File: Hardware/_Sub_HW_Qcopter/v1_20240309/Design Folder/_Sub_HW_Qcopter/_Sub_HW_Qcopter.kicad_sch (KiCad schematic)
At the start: 0 parts

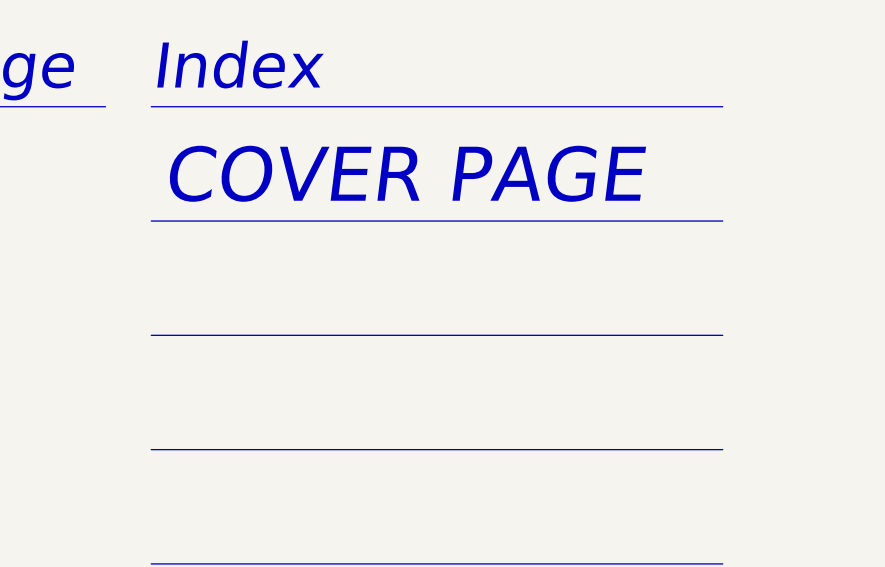
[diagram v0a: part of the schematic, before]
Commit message: The document structure of hardware has been added
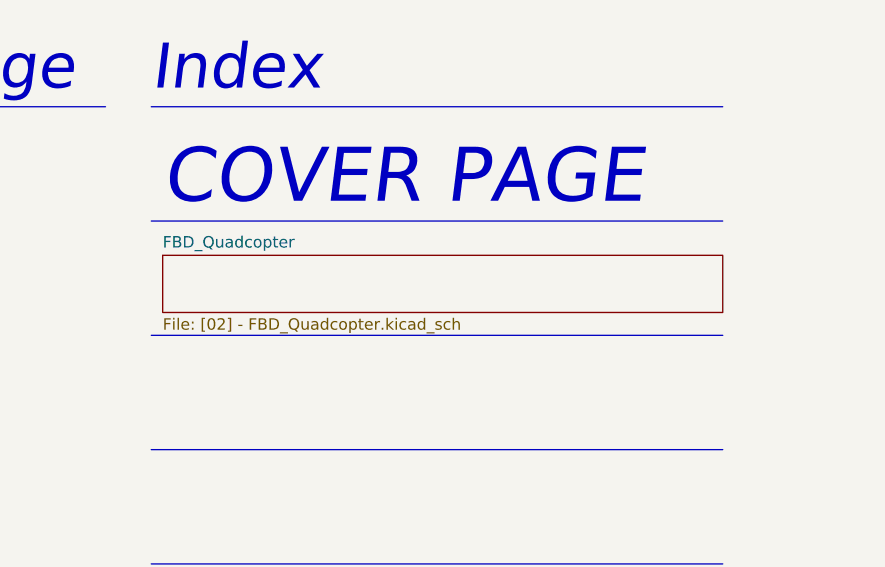
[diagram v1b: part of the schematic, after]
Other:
- added sheet FBD_Quadcopter ([02] - FBD_Quadcopter.kicad_sch)
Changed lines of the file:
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@@
+		)
+	)
+	(sheet
+		(at 64.77 118.11)
+		(size 62.23 6.35)
+		(fields_autoplaced yes)
+		(stroke
+			(width 0.1524)
+			(type solid)
+		)
+		(fill
+			(color 0 0 0 0.0000)
+		)
+		(property "Sheetname" "FBD_Quadcopter"
+			(at 64.77 117.3984 0)
+			(effects
+				(font
+					(size 1.27 1.27)
+				)
+				(justify left bottom)
+			)
+		)
+		(property "Sheetfile" "[02] - FBD_Quadcopter.kicad_sch"
+			(at 64.77 125.0446 0)
+			(effects
+				(font
+					(size 1.27 1.27)
+				)
+				(justify left top)
+			)
+		)
+		(instances
+			(project "_Sub_HW_Qcopter"
+				(path "/b8703f06-b3da-4de2-b217-f104939b36e8"
+					(page "2")
+				)
+			)
 		)
 	)

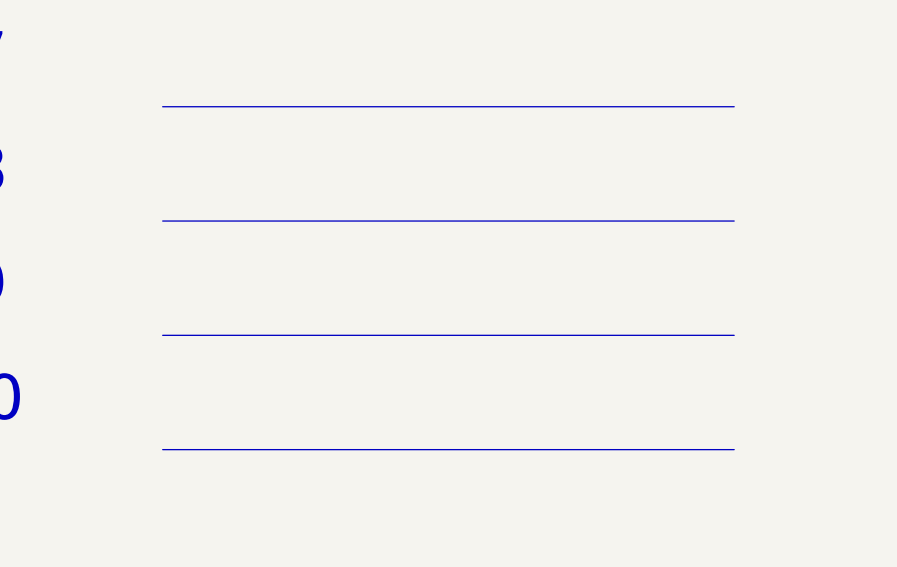
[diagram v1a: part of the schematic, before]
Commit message: Schematic is done by 90%
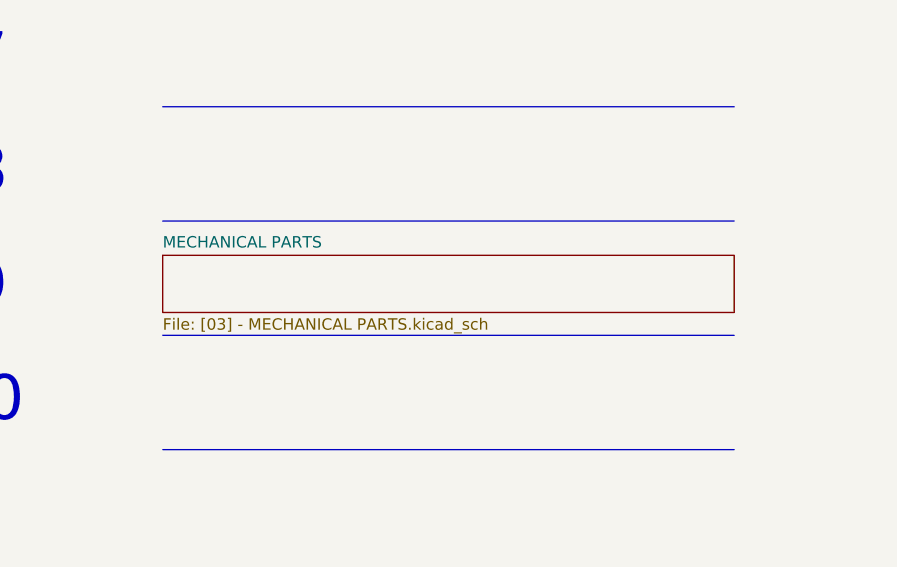
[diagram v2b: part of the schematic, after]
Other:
- added sheet MECHANICAL PARTS ([03] - MECHANICAL PARTS.kicad_sch)
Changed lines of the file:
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@@
+		)
+	)
+	(sheet
+		(at 63.5 207.01)
+		(size 63.5 6.35)
+		(fields_autoplaced yes)
+		(stroke
+			(width 0.1524)
+			(type solid)
+		)
+		(fill
+			(color 0 0 0 0.0000)
+		)
+		(property "Sheetname" "MECHANICAL PARTS"
+			(at 63.5 206.2984 0)
+			(effects
+				(font
+					(size 1.27 1.27)
+				)
+				(justify left bottom)
+			)
+		)
+		(property "Sheetfile" "[03] - MECHANICAL PARTS.kicad_sch"
+			(at 63.5 213.9446 0)
+			(effects
+				(font
+					(size 1.27 1.27)
+				)
+				(justify left top)
+			)
+		)
+		(instances
+			(project "_Sub_HW_Qcopter"
+				(path "/b8703f06-b3da-4de2-b217-f104939b36e8"
+					(page "24")
+				)
+			)
 		)
 	)
